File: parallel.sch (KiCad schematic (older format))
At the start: 75 parts, among them CN300 KEYBOARD, CN301 DB25F, CN302 DB23F, CN303 Conn_02x17_Odd_Even, J3 ACCEL, J300 Conn_01x03_Male, J301 DF1:, Q301 2N3904, U102 GARY5719, U108 74LS74A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

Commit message: Now with F DB23, connectors are ok
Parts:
- CN302: footprint d_amiga:DSUB-23_Male_Horizontal_P2.77x2.84mm_EdgePinOffset7.70mm_Housed_MountingHolesOffset9.12mm -> d_amiga:DSUB-23_Female_Horizontal_P2.77x2.84mm_EdgePinOffset7.70mm_Housed_MountingHolesOffset9.12mm
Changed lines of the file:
@@
 F 0 "CN302" V 12785 2450 50  0000 C CNN
 F 1 "DB23F" V 12876 2450 50  0000 C CNN
-F 2 "d_amiga:DSUB-23_Male_Horizontal_P2.77x2.84mm_EdgePinOffset7.70mm_Housed_MountingHolesOffset9.12mm" H 13100 2350 50  0001 C CNN
+F 2 "d_amiga:DSUB-23_Female_Horizontal_P2.77x2.84mm_EdgePinOffset7.70mm_Housed_MountingHolesOffset9.12mm" H 13100 2350 50  0001 C CNN
 F 3 " ~" H 13100 2350 50  0001 C CNN
 F 4 "Female" V 13150 2450 50  0001 C CNN "Gender"

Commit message: Switch footprints for suitable modern replacements
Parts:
- C203, C259, C260, C261, C300, C302, C303, C322, C323, C607, C909, C916: footprint Capacitor_THT:C_Rect_L11.5mm_W2.0mm_P10.00mm_MKT -> Capacitor_THT:C_Rect_L11.5mm_W2.6mm_P10.00mm_MKT
- C912: footprint Capacitor_THT:CP_Radial_D8.0mm_P5.00mm -> Capacitor_THT:CP_Radial_D10.0mm_P5.00mm
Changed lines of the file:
@@
 F 0 "C261" H 9115 1846 50  0000 L CNN
 F 1 "100pF" H 9115 1755 50  0000 L CNN
-F 2 "Capacitor_THT:C_Rect_L11.5mm_W2.0mm_P10.00mm_MKT" H 9038 1650 50  0001 C CNN
+F 2 "Capacitor_THT:C_Rect_L11.5mm_W2.6mm_P10.00mm_MKT" H 9038 1650 50  0001 C CNN
 F 3 "~" H 9000 1800 50  0001 C CNN
 	1    9000 1800
@@
 F 0 "C260" H 9565 1846 50  0000 L CNN
 F 1 "100pF" H 9565 1755 50  0000 L CNN
-F 2 "Capacitor_THT:C_Rect_L11.5mm_W2.0mm_P10.00mm_MKT" H 9488 1650 50  0001 C CNN
+F 2 "Capacitor_THT:C_Rect_L11.5mm_W2.6mm_P10.00mm_MKT" H 9488 1650 50  0001 C CNN
 F 3 "~" H 9450 1800 50  0001 C CNN
 	1    9450 1800
@@
 F 0 "C259" H 10015 1846 50  0000 L CNN
 F 1 "100pF" H 10015 1755 50  0000 L CNN
-F 2 "Capacitor_THT:C_Rect_L11.5mm_W2.0mm_P10.00mm_MKT" H 9938 1650 50  0001 C CNN
+F 2 "Capacitor_THT:C_Rect_L11.5mm_W2.6mm_P10.00mm_MKT" H 9938 1650 50  0001 C CNN
 F 3 "~" H 9900 1800 50  0001 C CNN
 	1    9900 1800
@@
 F 0 "C912" H 10468 1846 50  0000 L CNN
 F 1 "470uF 25v" H 10468 1755 50  0000 L CNN
-F 2 "Capacitor_THT:CP_Radial_D8.0mm_P5.00mm" H 10388 1650 50  0001 C CNN
+F 2 "Capacitor_THT:CP_Radial_D10.0mm_P5.00mm" H 10388 1650 50  0001 C CNN
 F 3 "~" H 10350 1800 50  0001 C CNN
 	1    10350 1800
@@
 F 0 "C909" H 3415 6046 50  0000 L CNN
 F 1 "0.1uF" H 3415 5955 50  0000 L CNN
-F 2 "Capacitor_THT:C_Rect_L11.5mm_W2.0mm_P10.00mm_MKT" H 3338 5850 50  0001 C CNN
+F 2 "Capacitor_THT:C_Rect_L11.5mm_W2.6mm_P10.00mm_MKT" H 3338 5850 50  0001 C CNN
 F 3 "~" H 3300 6000 50  0001 C CNN
 	1    3300 6000
@@
 F 0 "C916" H 8215 7446 50  0000 L CNN
 F 1 "0.1uF" H 8215 7355 50  0000 L CNN
-F 2 "Capacitor_THT:C_Rect_L11.5mm_W2.0mm_P10.00mm_MKT" H 8138 7250 50  0001 C CNN
+F 2 "Capacitor_THT:C_Rect_L11.5mm_W2.6mm_P10.00mm_MKT" H 8138 7250 50  0001 C CNN
 F 3 "~" H 8100 7400 50  0001 C CNN
 	1    8100 7400
@@
 F 0 "C322" H 15265 2046 50  0000 L CNN
 F 1 "0.01uF" H 15265 1955 50  0000 L CNN
-F 2 "Capacitor_THT:C_Rect_L11.5mm_W2.0mm_P10.00mm_MKT" H 15188 1850 50  0001 C CNN
+F 2 "Capacitor_THT:C_Rect_L11.5mm_W2.6mm_P10.00mm_MKT" H 15188 1850 50  0001 C CNN
 F 3 "~" H 15150 2000 50  0001 C CNN
 	1    15150 2000
@@
 F 0 "C323" H 15765 2046 50  0000 L CNN
 F 1 "0.01uF" H 15765 1955 50  0000 L CNN
-F 2 "Capacitor_THT:C_Rect_L11.5mm_W2.0mm_P10.00mm_MKT" H 15688 1850 50  0001 C CNN
+F 2 "Capacitor_THT:C_Rect_L11.5mm_W2.6mm_P10.00mm_MKT" H 15688 1850 50  0001 C CNN
 F 3 "~" H 15650 2000 50  0001 C CNN
 	1    15650 2000
@@
 F 0 "C300" H 2865 2846 50  0000 L CNN
 F 1 "0.1uF" H 2865 2755 50  0000 L CNN
-F 2 "Capacitor_THT:C_Rect_L11.5mm_W2.0mm_P10.00mm_MKT" H 2788 2650 50  0001 C CNN
+F 2 "Capacitor_THT:C_Rect_L11.5mm_W2.6mm_P10.00mm_MKT" H 2788 2650 50  0001 C CNN
 F 3 "~" H 2750 2800 50  0001 C CNN
 	1    2750 2800
@@
 F 0 "C203" H 2815 10046 50  0000 L CNN
 F 1 "0.1uF" H 2815 9955 50  0000 L CNN
-F 2 "Capacitor_THT:C_Rect_L11.5mm_W2.0mm_P10.00mm_MKT" H 2738 9850 50  0001 C CNN
+F 2 "Capacitor_THT:C_Rect_L11.5mm_W2.6mm_P10.00mm_MKT" H 2738 9850 50  0001 C CNN
 F 3 "~" H 2700 10000 50  0001 C CNN
 	1    2700 10000
@@
 F 0 "C302" H 4515 10046 50  0000 L CNN
 F 1 "0.1uF" H 4515 9955 50  0000 L CNN
-F 2 "Capacitor_THT:C_Rect_L11.5mm_W2.0mm_P10.00mm_MKT" H 4438 9850 50  0001 C CNN
+F 2 "Capacitor_THT:C_Rect_L11.5mm_W2.6mm_P10.00mm_MKT" H 4438 9850 50  0001 C CNN
 F 3 "~" H 4400 10000 50  0001 C CNN
 	1    4400 10000
@@
 F 0 "C303" H 6215 10046 50  0000 L CNN
 F 1 "0.1uF" H 6215 9955 50  0000 L CNN
-F 2 "Capacitor_THT:C_Rect_L11.5mm_W2.0mm_P10.00mm_MKT" H 6138 9850 50  0001 C CNN
+F 2 "Capacitor_THT:C_Rect_L11.5mm_W2.6mm_P10.00mm_MKT" H 6138 9850 50  0001 C CNN
 F 3 "~" H 6100 10000 50  0001 C CNN
 	1    6100 10000
@@
 F 0 "C607" H 7715 9996 50  0000 L CNN
 F 1 "0.1uF" H 7715 9905 50  0000 L CNN
-F 2 "Capacitor_THT:C_Rect_L11.5mm_W2.0mm_P10.00mm_MKT" H 7638 9800 50  0001 C CNN
+F 2 "Capacitor_THT:C_Rect_L11.5mm_W2.6mm_P10.00mm_MKT" H 7638 9800 50  0001 C CNN
 F 3 "~" H 7600 9950 50  0001 C CNN
 	1    7600 9950

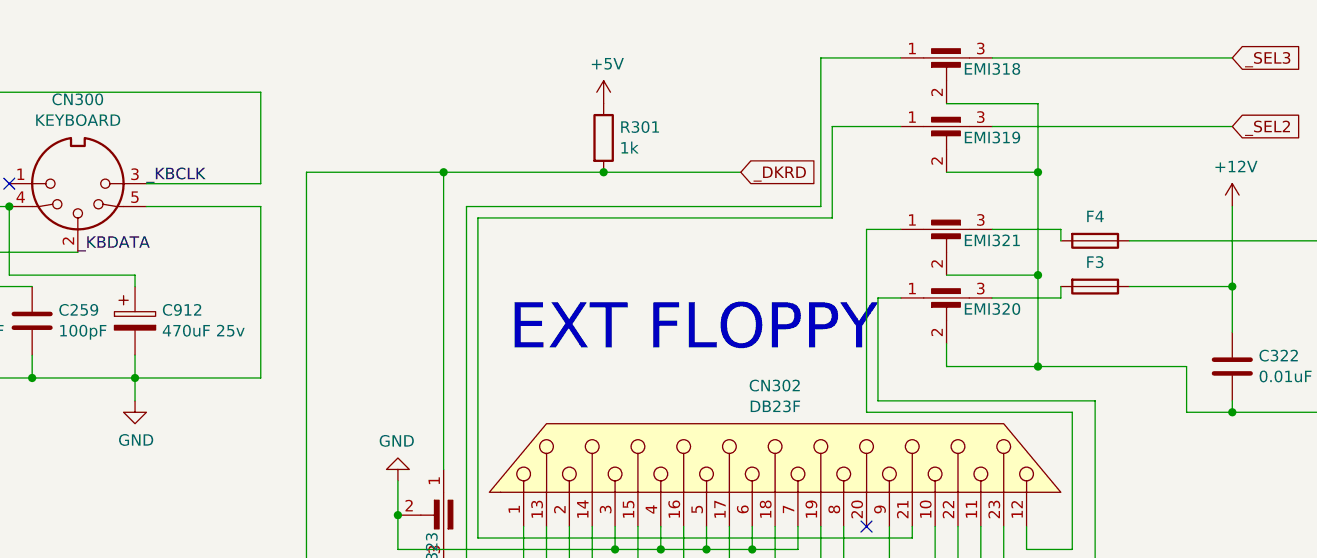
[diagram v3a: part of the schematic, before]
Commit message: Some footprints updates; Add all Mouser references
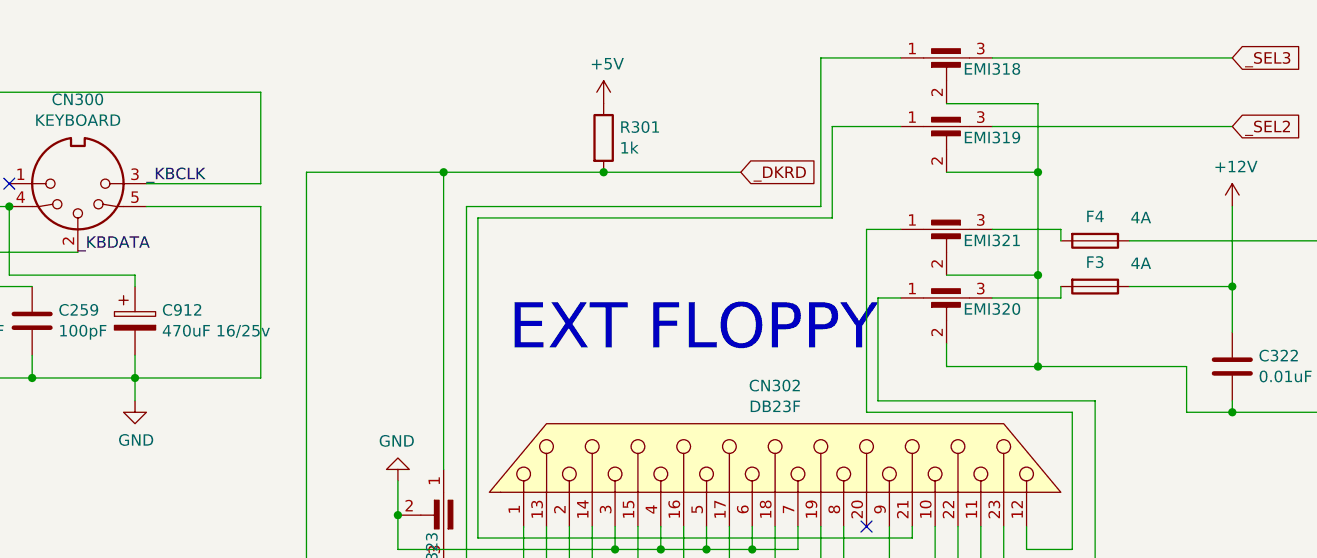
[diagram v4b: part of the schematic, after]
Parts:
- C203, C300, C302, C303, C607, C909, C916: RefOrder (none) -> 581-SA105C104KARC
- C259, C260, C261: RefOrder (none) -> 80-C410C101K5G
- C322, C323: RefOrder (none) -> 581-SA105C103K
- C912: value 470uF 25v -> 470uF 16/25v; RefOrder (none) -> 647-UVR1E471MPD
- EMI300, EMI301, EMI302, EMI303, EMI304, EMI305, EMI306, EMI307, EMI308, EMI309, EMI310, EMI335, EMI336, EMI337, EMI338: value C_Feedthrough -> 330pF (Type F 331); RefOrder (none) -> 81-DSS1NB32A331Q91A
- EMI311, EMI312, EMI313, EMI314, EMI315, EMI316, EMI317, EMI318, EMI319, EMI320, EMI321: value C_Feedthrough -> 100pF (Type F 101); RefOrder (none) -> 81-DSS1NB32A101Q91A
- EMI322, EMI323, EMI324, EMI339, EMI340, EMI341: value C_Feedthrough -> 100pF (Type C 101); RefOrder (none) -> Using Type F instead 81-DSS1NB32A101Q91A
- F3, F4: value Fuse -> 4A; RefOrder (none) -> 576-0251004.MRT1L
- FB301, FB302, FB303: RefOrder (none) -> 875-28L0138-10R-10
- Q301: RefOrder (none) -> 833-2N3904-AP
- R201, R300, R309: RefOrder (none) -> 603-CFR-25JT-52-4K7
- R301, R602: RefOrder (none) -> 603-CFR-25JR-521K
- R310: RefOrder (none) -> 588-OL4705E-R52
- R914: RefOrder (none) -> 603-CFR-50JB-52-1R
- RP300: RefOrder (none) -> 652-4610X-1LF-10K
- RP301: RefOrder (none) -> 652-4606M-1LF-1K
- U108: RefOrder (none) -> 595-SN74LS74AN
- U203: RefOrder (none) -> 595-SN74LS38N
- U302: RefOrder (none) -> 595-SN74LS32N
- U303: RefOrder (none) -> 595-SN74F08N
- U607: RefOrder (none) -> 595-SN74LS08N
- U900: RefOrder (none) -> 595-SN74F00N
